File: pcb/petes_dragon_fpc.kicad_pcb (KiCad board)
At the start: 2 copper layers, 190 x 160 mm, 200 parts

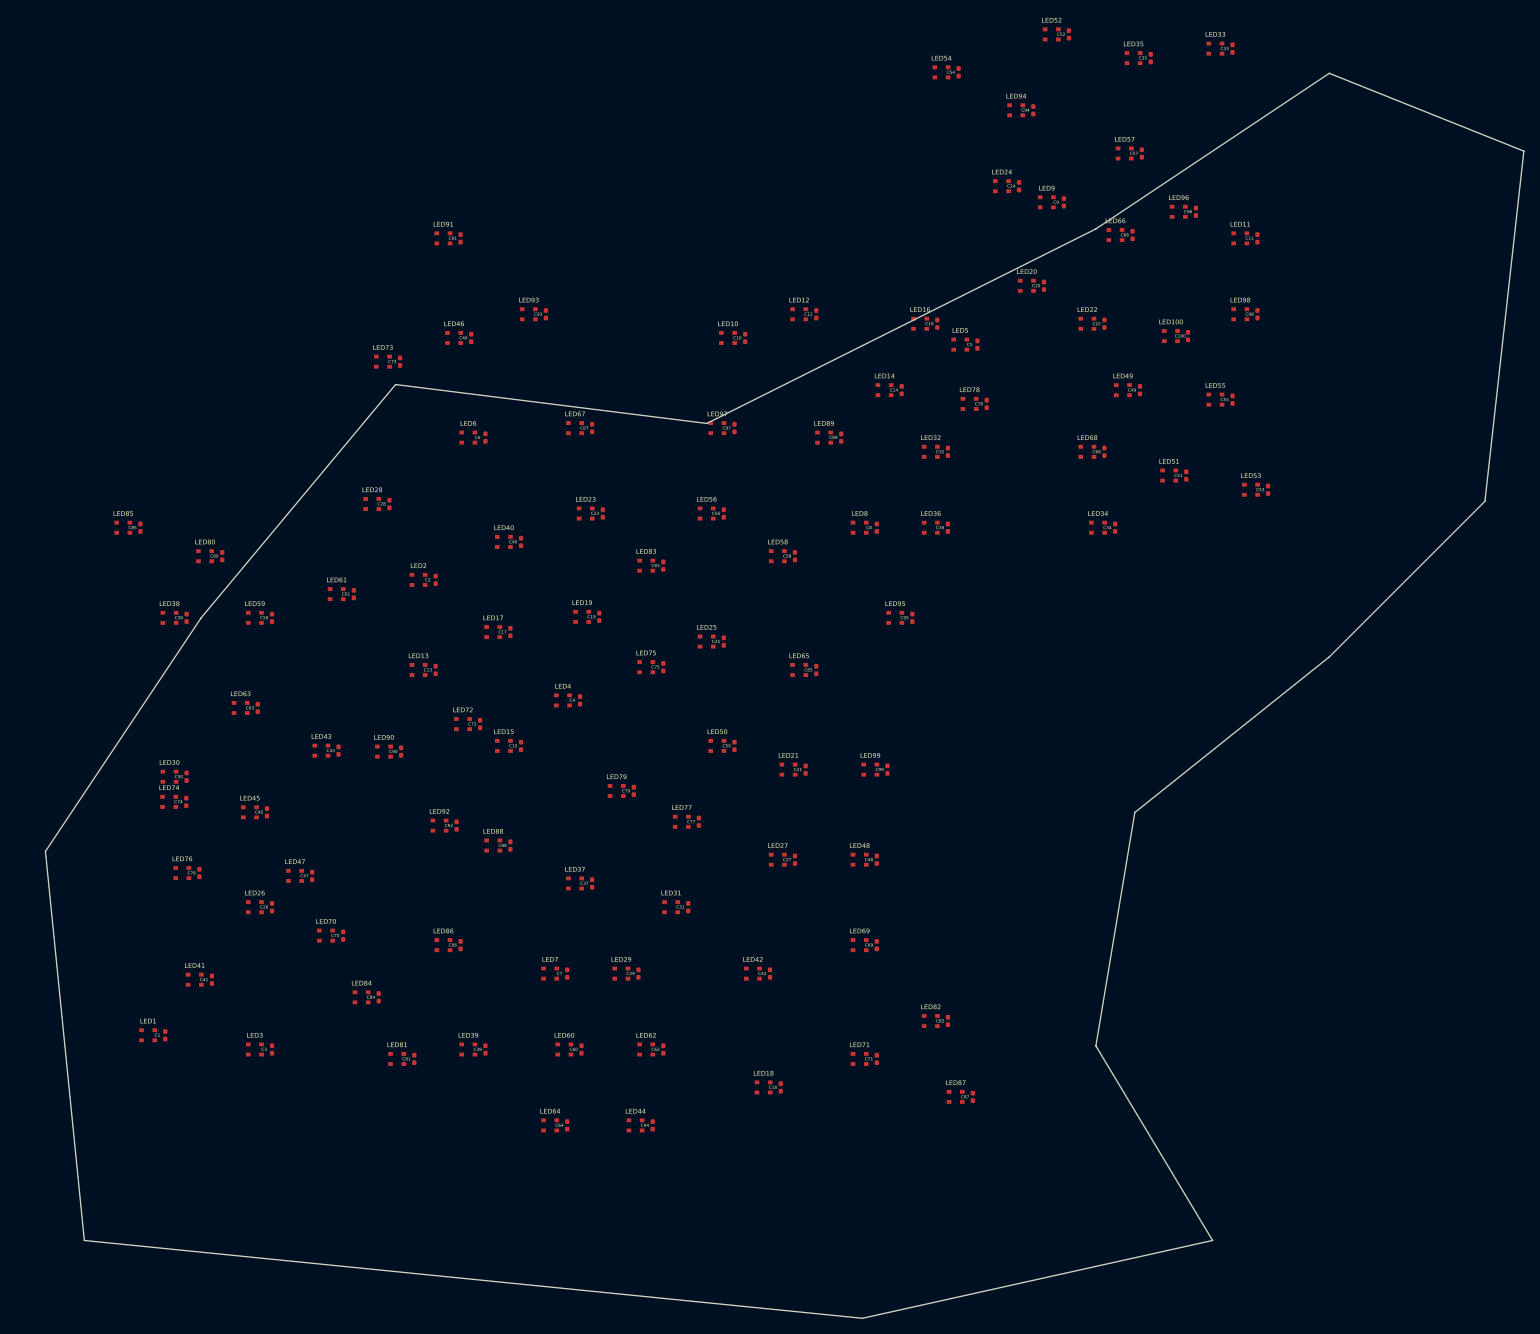
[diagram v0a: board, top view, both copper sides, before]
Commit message: fix: calibrate PCB preview and layout coordinates to 1:1 coincident alignment with dragon artwork
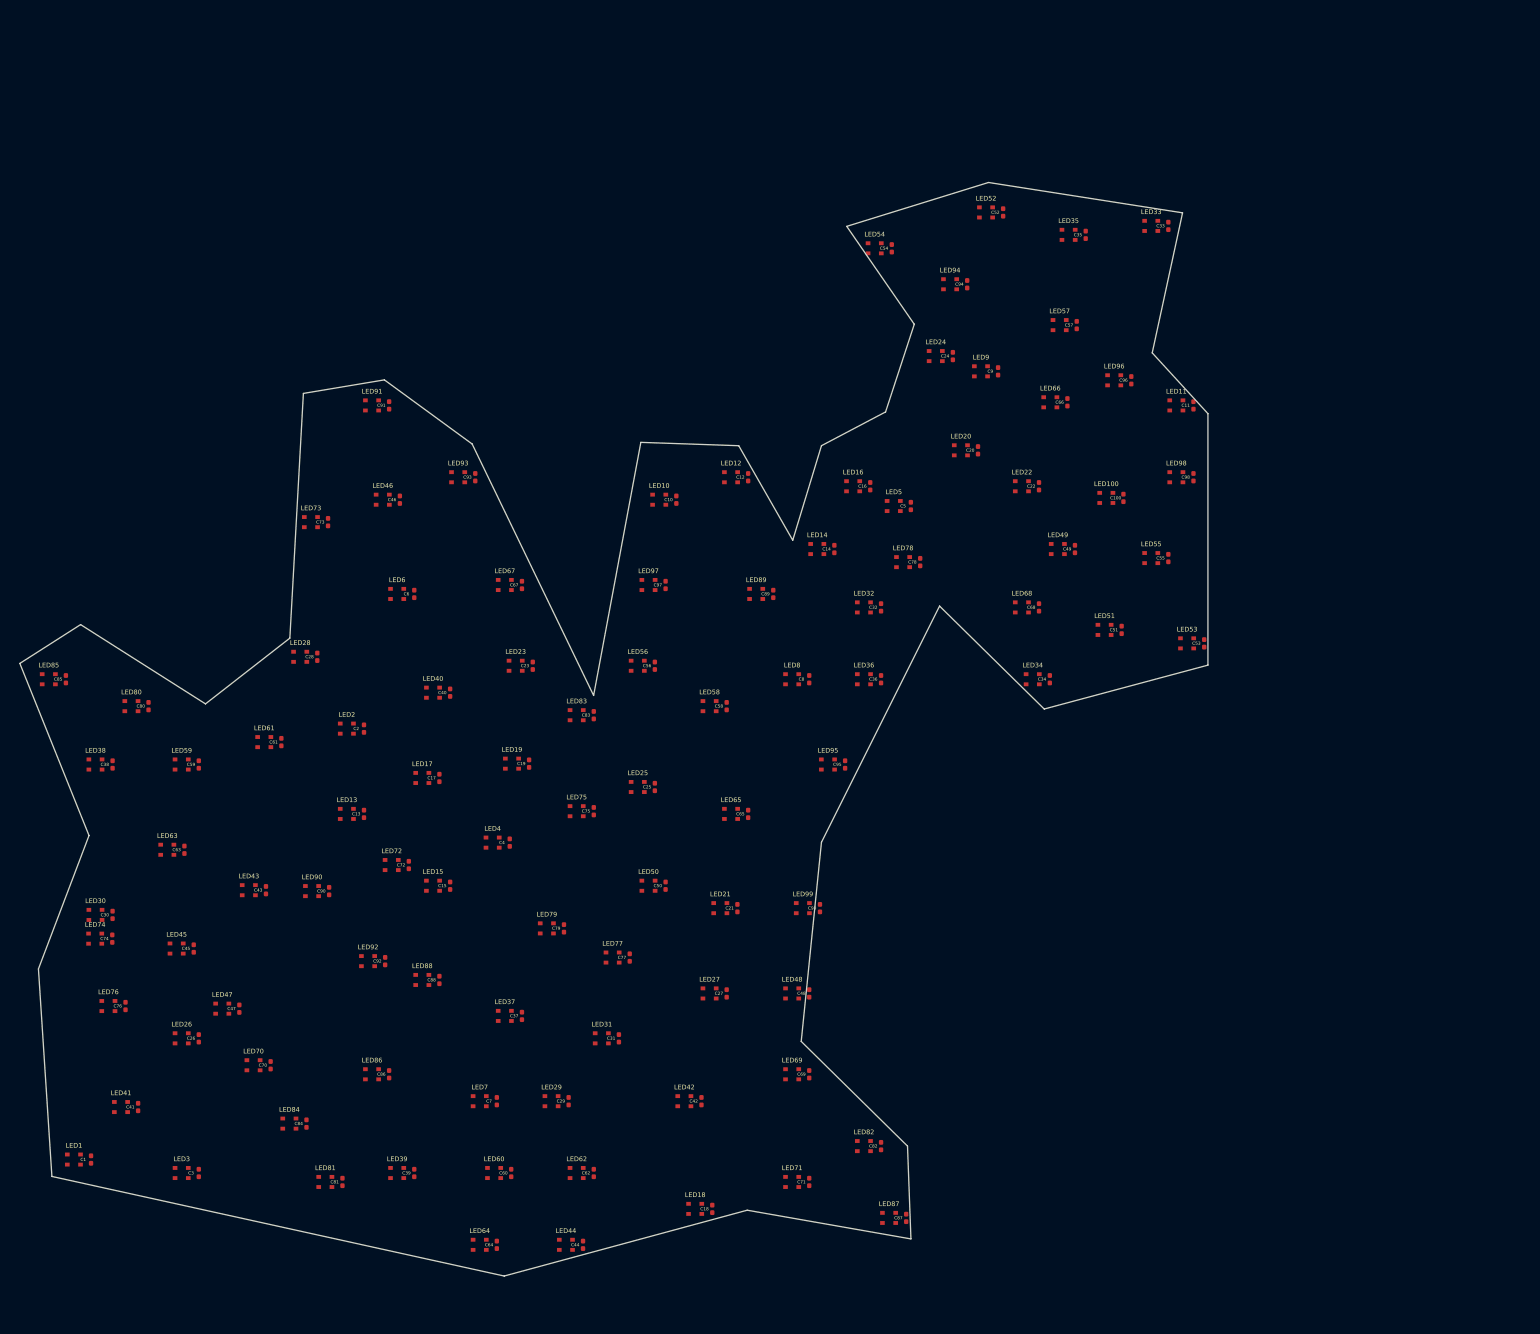
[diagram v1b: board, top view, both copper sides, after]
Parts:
- moved LED52 24.4 mm to (135.9, 47.9)
- moved C52 24.4 mm to (138.1, 47.9)
- moved C33 24.2 mm to (159.3, 49.6)
- moved LED33 24.2 mm to (157.1, 49.6)
- moved C35 24.2 mm to (148.7, 50.8)
- moved LED35 24.2 mm to (146.5, 50.8)
- moved LED54 24.2 mm to (121.6, 52.5)
- moved C54 24.2 mm to (123.8, 52.5)
- moved LED94 23.9 mm to (131.3, 57.1)
- moved C94 23.9 mm to (133.5, 57.1)
- moved C57 23.6 mm to (147.5, 62.4)
- moved LED57 23.6 mm to (145.3, 62.4)
- moved LED24 23.4 mm to (129.4, 66.3)
- moved C24 23.4 mm to (131.6, 66.3)
- moved C91 23.3 mm to (59.2, 72.7)
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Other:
- board size 190 x 160 mm -> 152.7 x 140.5 mm

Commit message: feat(pcb): optimize daisy-chain traces with 2-opt nearest-neighbor routing
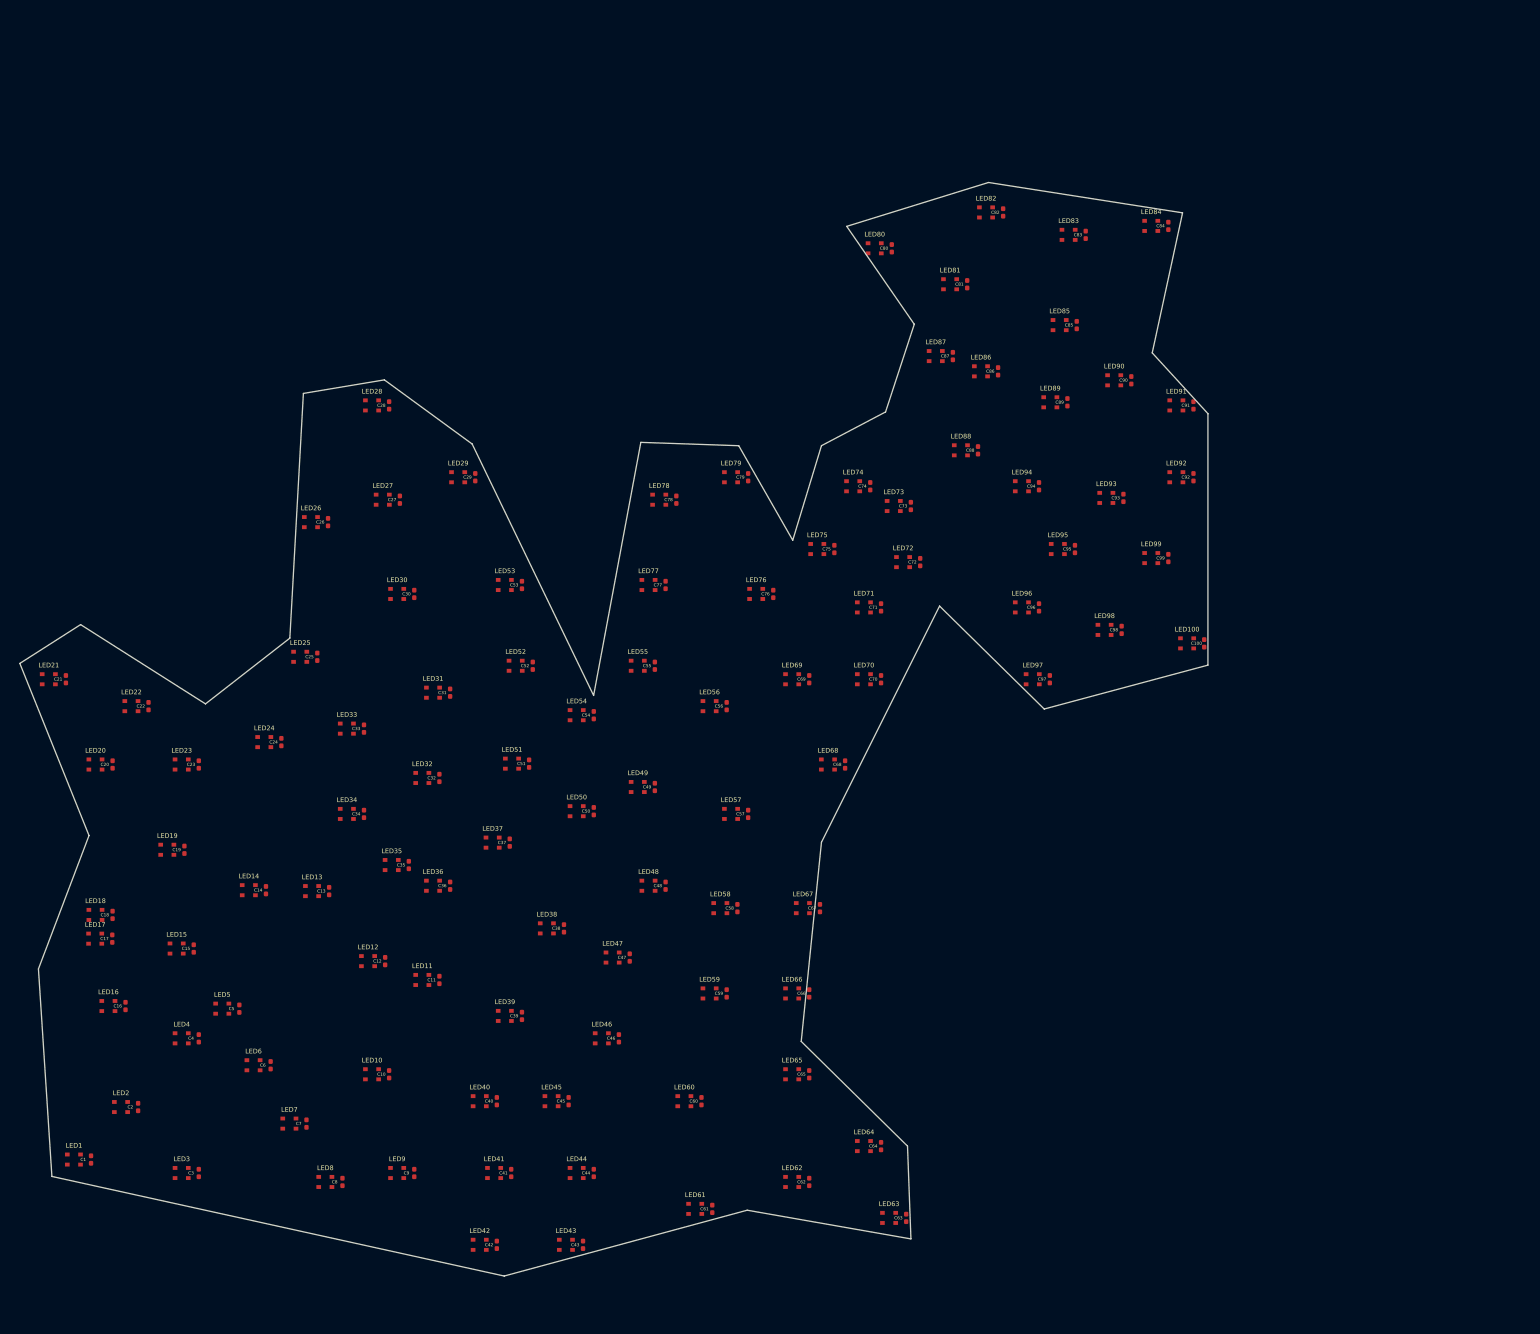
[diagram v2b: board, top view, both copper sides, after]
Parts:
- moved C84 159.9 mm to (159.3, 49.6)
- moved LED84 159.9 mm to (157.1, 49.6)
- moved C81 140.6 mm to (133.5, 57.1)
- moved LED81 140.6 mm to (131.3, 57.1)
- moved C85 137.7 mm to (147.5, 62.4)
- moved LED85 137.7 mm to (145.3, 62.4)
- moved C9 127.5 mm to (62.4, 171.3)
- moved LED9 127.5 mm to (60.2, 171.3)
- moved C90 122.2 mm to (154.6, 69.5)
- moved LED90 122.2 mm to (152.3, 69.5)
- moved C33 121.9 mm to (55.9, 114.2)
- moved LED33 121.9 mm to (53.7, 114.2)
- moved C11 121.8 mm to (65.6, 146.5)
- moved LED11 121.8 mm to (63.4, 146.5)
- moved C92 121.1 mm to (162.5, 81.9)
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
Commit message: fix(pcb): enforce boundary-constrained routing to prevent traces leaving PCB outline
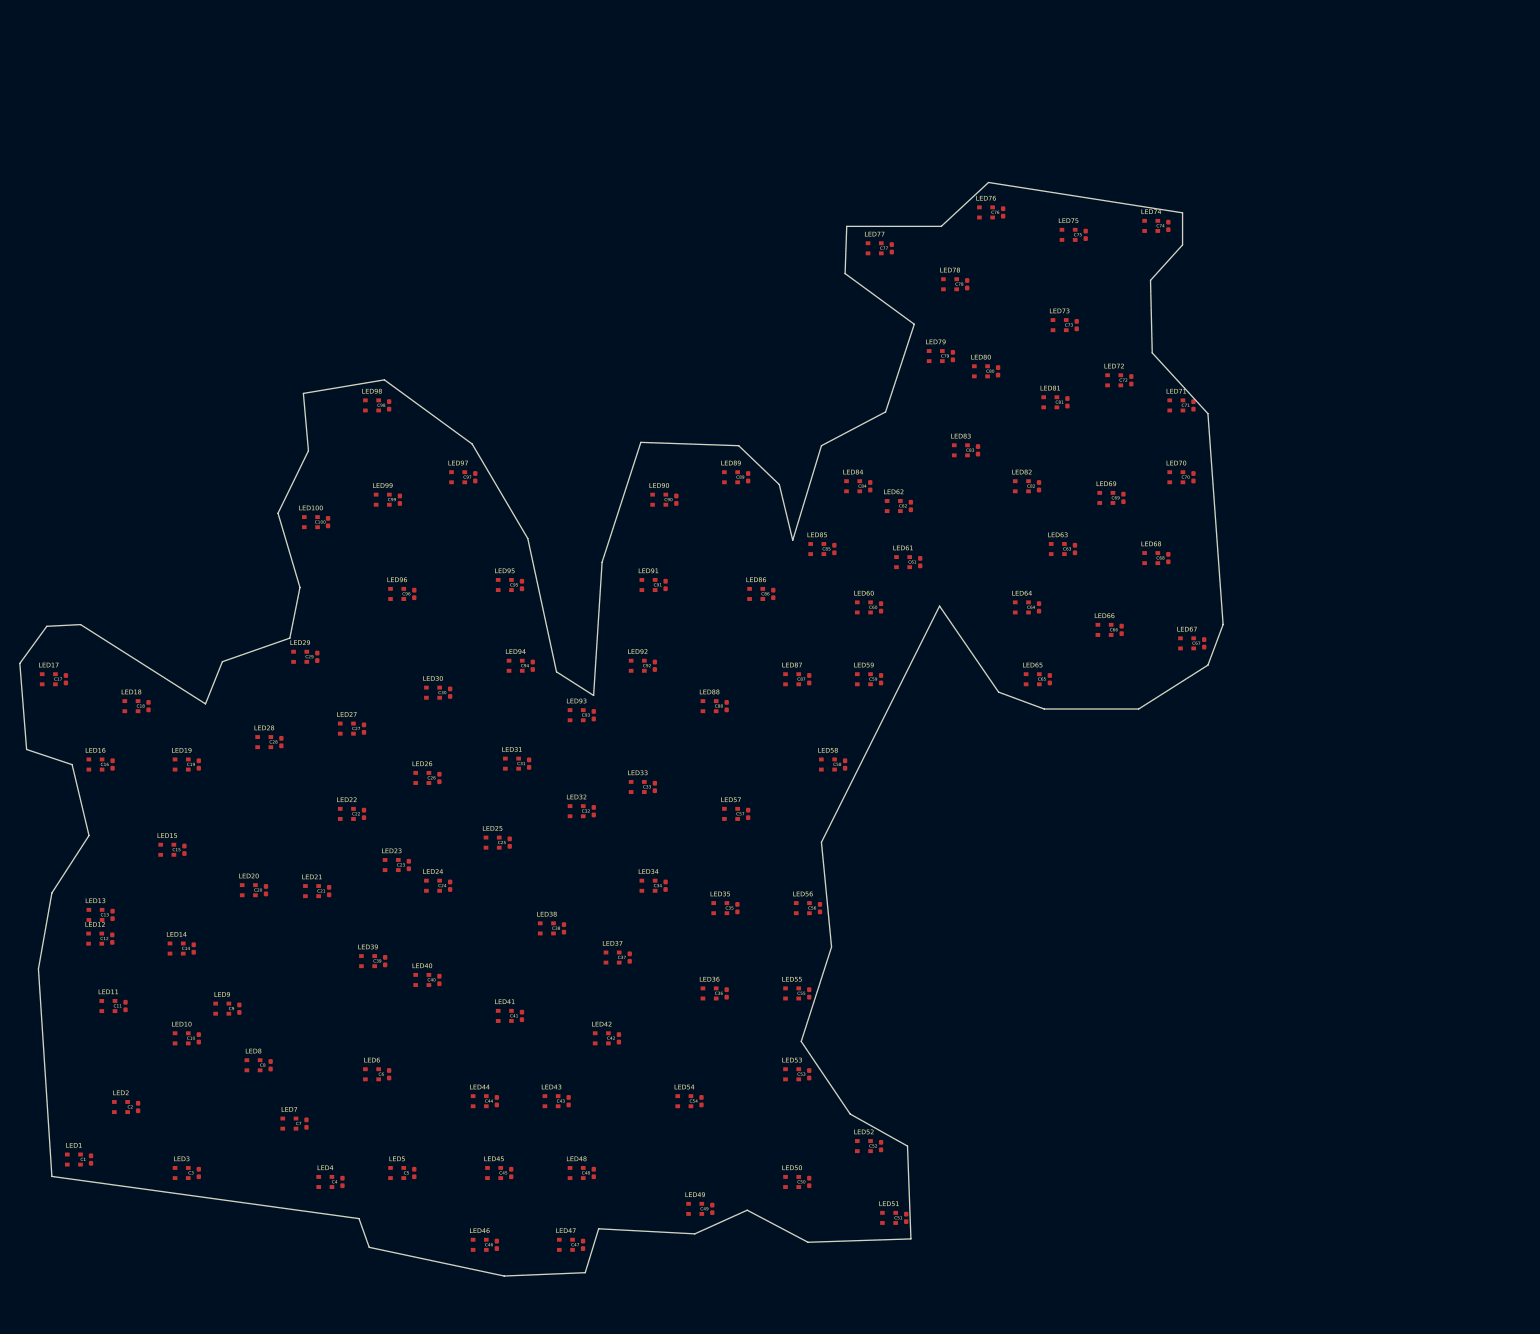
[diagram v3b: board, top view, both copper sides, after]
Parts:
- moved C100 113.7 mm to (51.3, 87.7)
- moved LED100 113.7 mm to (49.1, 87.7)
- moved LED99 99.0 mm to (58.4, 84.8)
- moved C99 99.0 mm to (60.5, 84.8)
- moved LED98 98.5 mm to (57.0, 72.7)
- moved C98 98.5 mm to (59.2, 72.7)
- moved C63 88.7 mm to (147.3, 91.1)
- moved LED63 88.7 mm to (145.1, 91.1)
- moved C62 87.8 mm to (126.2, 85.6)
- moved LED62 87.8 mm to (124.0, 85.6)
- moved C61 87.3 mm to (127.4, 92.8)
- moved LED61 87.3 mm to (125.2, 92.8)
- moved LED96 80.3 mm to (60.2, 96.9)
- moved C96 80.3 mm to (62.4, 96.9)
- moved C97 78.3 mm to (70.2, 81.9)
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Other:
- board size 152.7 x 140.5 mm -> 154.6 x 140.5 mm
